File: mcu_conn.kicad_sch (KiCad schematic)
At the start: 38 parts, among them J11 MD_MCU_PU_EN, J9 MD_MCU_EN, Q6 FDV305N, U2 Teensy4.1, U3 INA190A5IDDFR, U4 INA190A5IDDFR

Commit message: Add noise amplifier sheet, fill part fields, consolidate 10u and 100n caps
Noise amplifier: OPA4388 with three x11 stages, outputs at x121 and x1331
on J16 and J17, enabled by J15. Footprints and part fields on all its parts.
C2 moves to the same 0805 100n as the other 0.1u caps. Every 10u except the
C3 and C4 compensation pair moves to the 10% Murata GRM319R61E106KA12D.

Co-Authored-By: Claude Opus 5.5 (1M context) <noreply@anthropic.com>
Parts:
- C20, C5: Distributer Link 1 https://www.digikey.com/en/products/detail/kemet/C1206C106J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 -> https://www.digikey.com/en/products/detail/murata-electroni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; Manufacturer KEMET -> Murata Electronics; Manufacturer Part Number C1206C106J3RACAUTO -> GRM319R61E106KA12D
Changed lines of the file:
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@@
 			)
 		)
-		(property "Datasheet" "https://yageogroup.com/content/datasheet/asset/file/KEM_C1023_X7R_AUTO_SMD"
+		(property "Datasheet" "https://mm.digikey.com/Volume0/opasdata/d220001/medias/docus/8942/490_Chip_Multilayer_CAT2021_MLCC.pdf"
 			(at 123.19 179.07 0)
 			(hide yes)
@@
 			)
 		)
-		(property "Description" "CAP CER 10UF 5% 25V X7R 1206"
+		(property "Description" "CAP CER 10UF 25V X5R 1206"
 			(at 123.19 179.07 0)
 			(hide yes)
@@
 			)
 		)
-		(property "Manufacturer" "KEMET"
+		(property "Manufacturer" "Murata Electronics"
 			(at 123.19 179.07 0)
 			(hide yes)
@@
 			)
 		)
-		(property "Manufacturer Part Number" "C1206C106J3RACAUTO"
+		(property "Manufacturer Part Number" "GRM319R61E106KA12D"
 			(at 123.19 179.07 0)
 			(hide yes)
@@
 			)
 		)
-		(property "Distributer Link 1" "https://www.digikey.com/en/products/detail/kemet/C1206C106J3RACAUTO/7427564"
+		(property "Distributer Link 1" "https://www.digikey.com/en/products/detail/murata-electronics/GRM319R61E106KA12D/2334876"
 			(at 123.19 179.07 0)
 			(hide yes)
@@
 			)
 		)
-		(property "Datasheet" "https://yageogroup.com/content/datasheet/asset/file/KEM_C1023_X7R_AUTO_SMD"
+		(property "Datasheet" "https://mm.digikey.com/Volume0/opasdata/d220001/medias/docus/8942/490_Chip_Multilayer_CAT2021_MLCC.pdf"
 			(at 123.19 137.16 0)
 			(hide yes)
@@
 			)
 		)
-		(property "Description" "CAP CER 10UF 5% 25V X7R 1206"
+		(property "Description" "CAP CER 10UF 25V X5R 1206"
 			(at 123.19 137.16 0)
 			(hide yes)
@@
 			)
 		)
-		(property "Manufacturer" "KEMET"
+		(property "Manufacturer" "Murata Electronics"
 			(at 123.19 137.16 0)
 			(hide yes)
@@
 			)
 		)
-		(property "Manufacturer Part Number" "C1206C106J3RACAUTO"
+		(property "Manufacturer Part Number" "GRM319R61E106KA12D"
 			(at 123.19 137.16 0)
 			(hide yes)
@@
 			)
 		)
-		(property "Distributer Link 1" "https://www.digikey.com/en/products/detail/kemet/C1206C106J3RACAUTO/7427564"
+		(property "Distributer Link 1" "https://www.digikey.com/en/products/detail/murata-electronics/GRM319R61E106KA12D/2334876"
 			(at 123.19 137.16 0)
 			(hide yes)

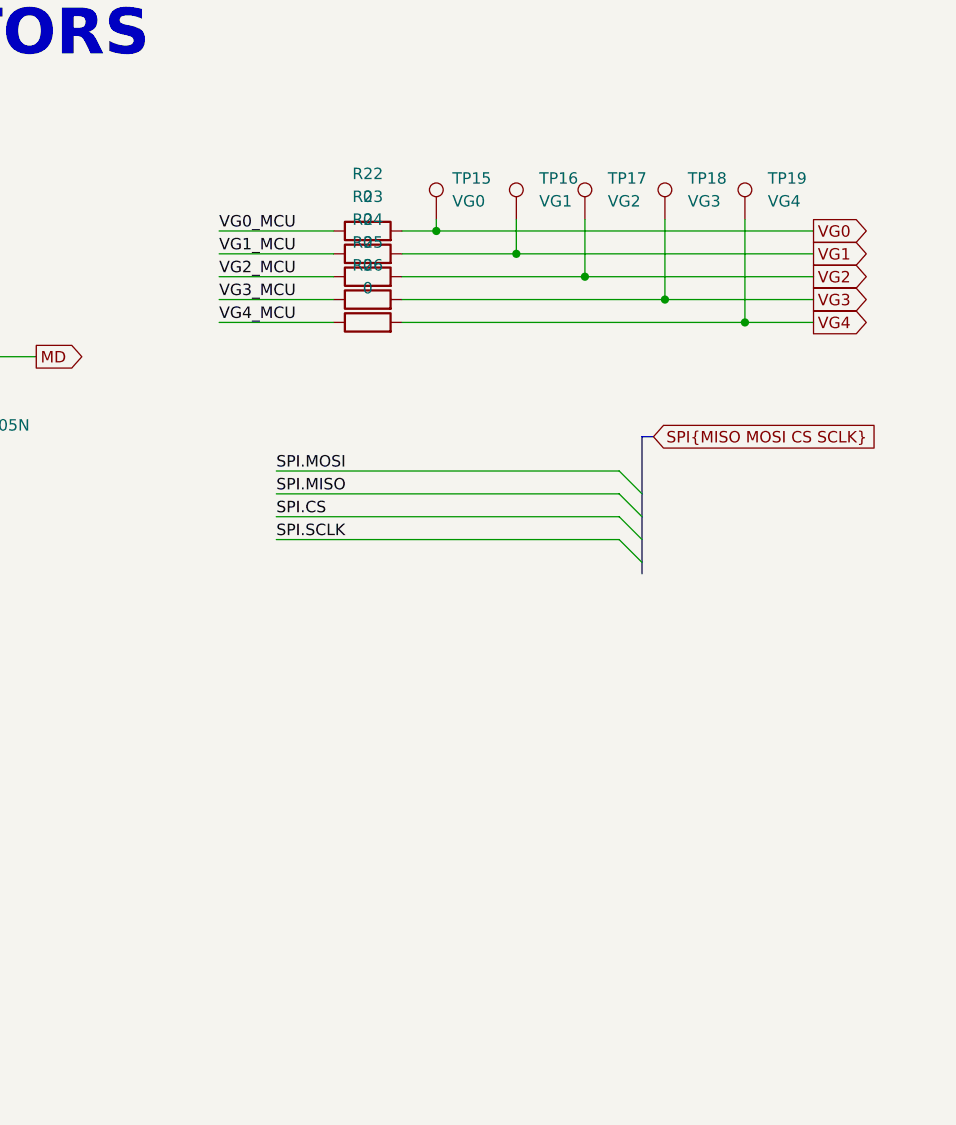
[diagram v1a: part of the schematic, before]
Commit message: Add ADT7310 SPI temperature sensor on the temperature sheet
U7 ADT7310TRZ (SOIC-8) on the shared SPI bus: SCLK, MOSI, MISO and CS to
Teensy pins 13, 11, 12 and 10. Powered from +3V3 with C31 100n at VDD.
INT and CT are left unconnected. New ADT7310TRZ symbol in the project
library, pinout from the ADT7310 datasheet Rev. A, page 6.

Co-Authored-By: Claude Opus 5.5 (1M context) <noreply@anthropic.com>
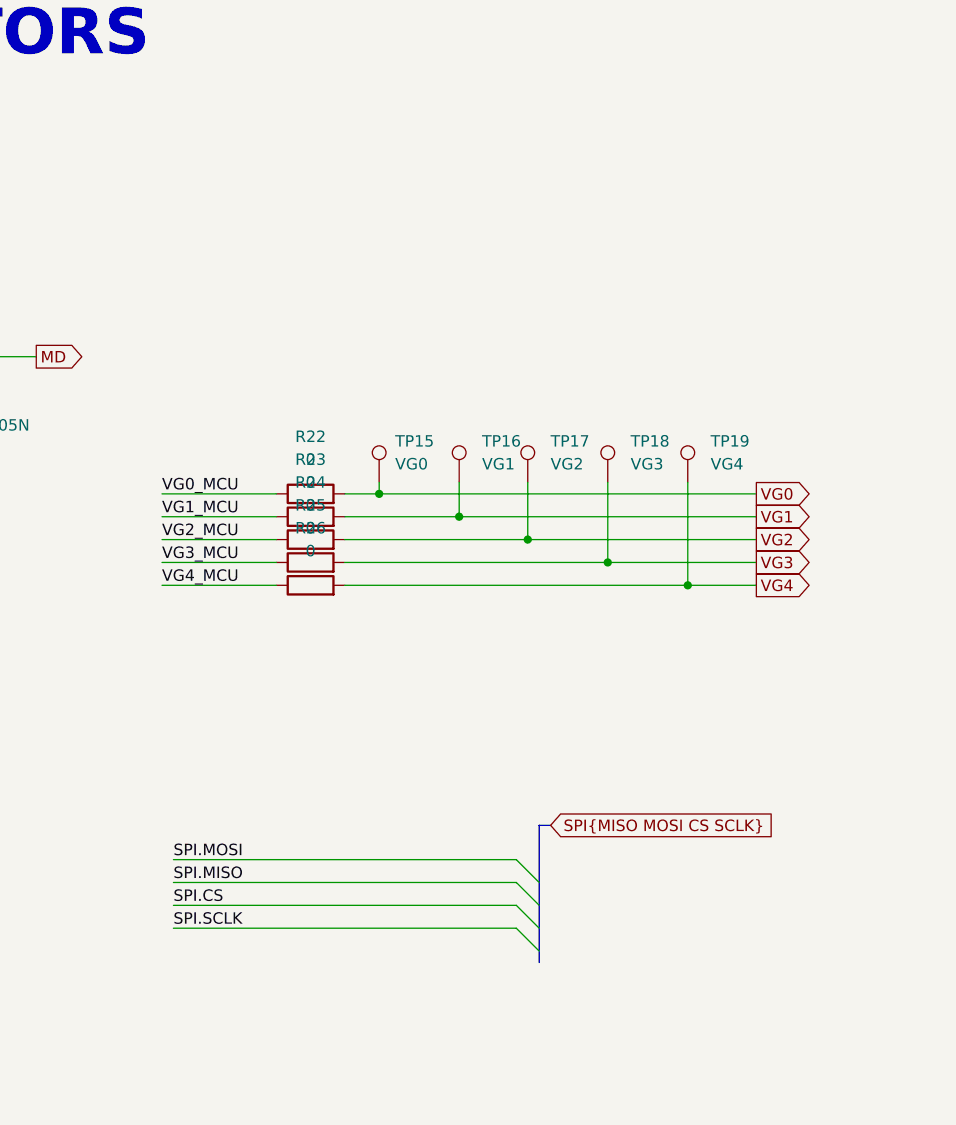
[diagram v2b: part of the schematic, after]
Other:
- moved on the sheet: R22, R23, R24, R25, R26, TP15, TP16, TP17, TP18, TP19
